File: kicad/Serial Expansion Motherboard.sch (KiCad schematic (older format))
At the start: 0 parts

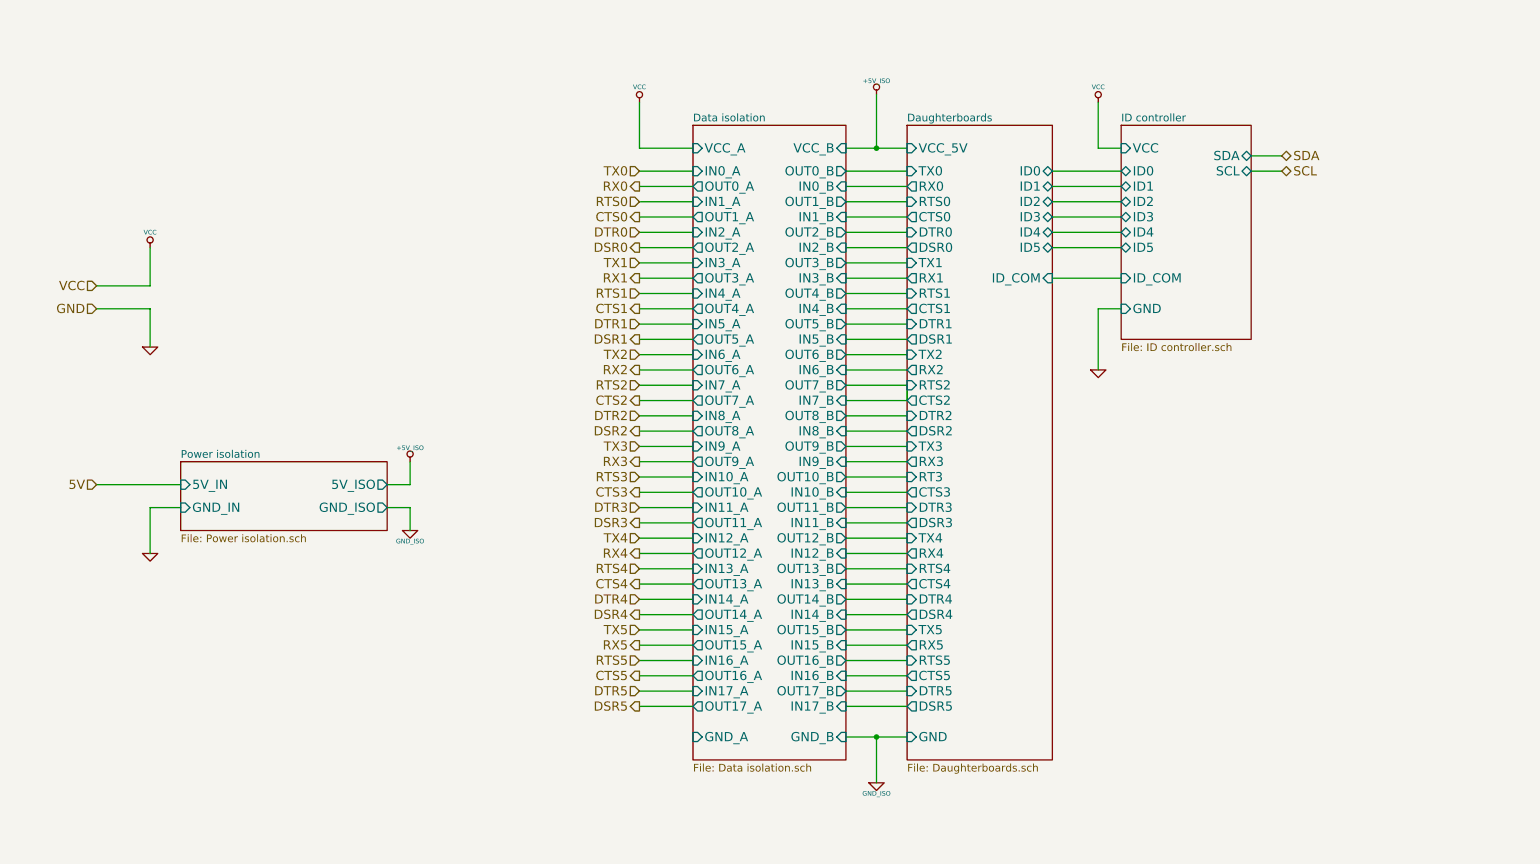
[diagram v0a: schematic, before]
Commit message: Completed data and power isolation sheets
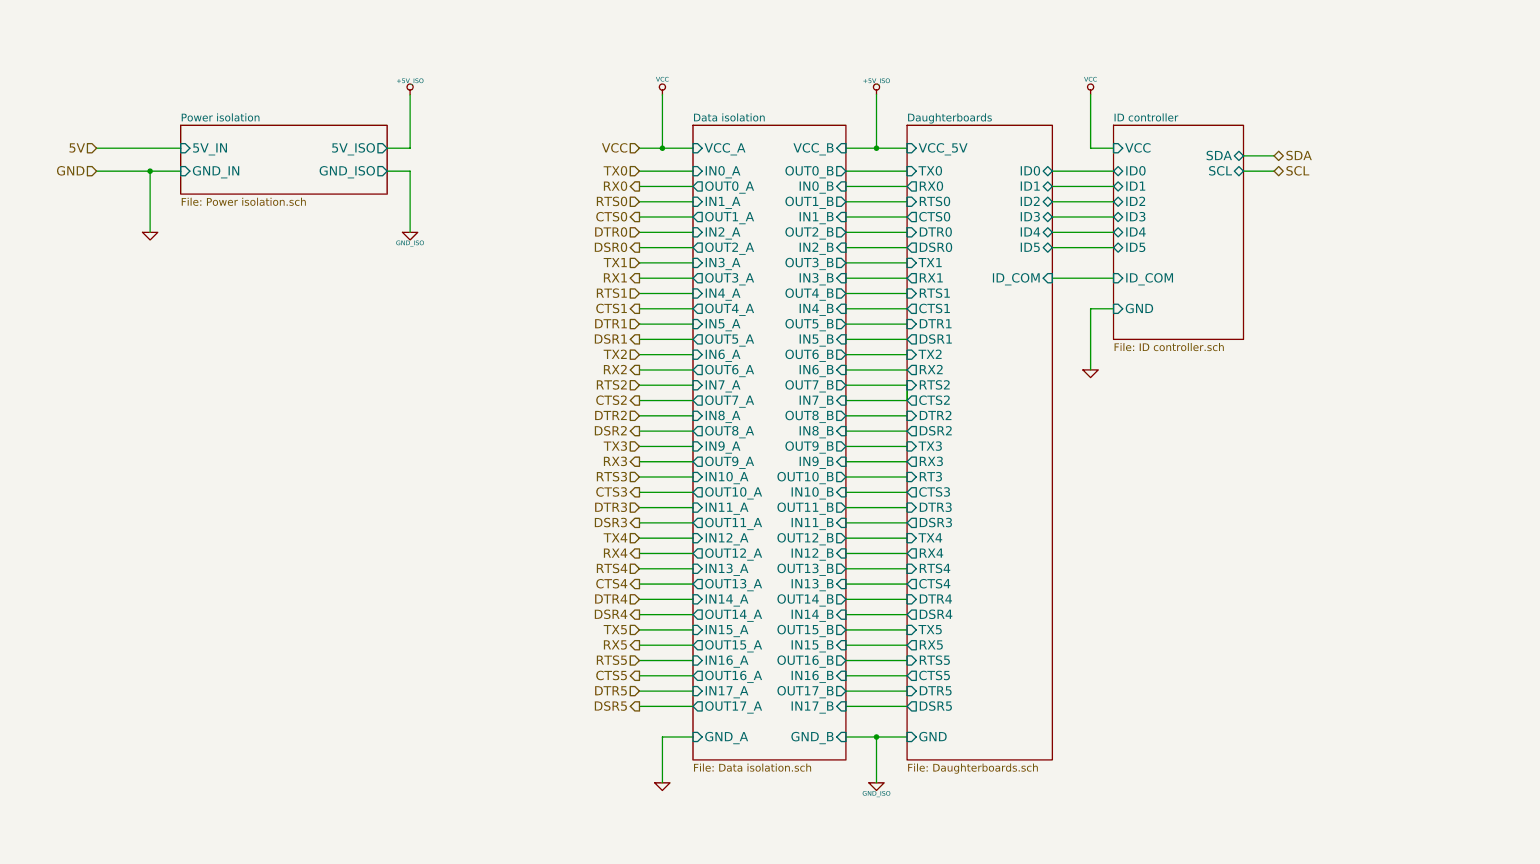
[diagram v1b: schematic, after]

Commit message: ID controller complete, bypass caps added in data isolation
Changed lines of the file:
@@
 LIBS:roe-0505s
 LIBS:si8660
+LIBS:pic16f1704
 LIBS:Main-cache
 EELAYER 27 0
@@
 	5550 5450 5200 5450
 Wire Wire Line
-	5550 1900 5350 1900
-Wire Wire Line
-	5350 1900 5200 1900
+	5200 1900 5550 1900
 Wire Wire Line
 	5550 2150 5200 2150
@@
 	6950 5550 6550 5550
 Wire Wire Line
-	6550 5750 6750 5750
-Wire Wire Line
-	6750 5750 6950 5750
+	6550 5750 6950 5750
 Wire Wire Line
 	7900 2050 8300 2050
@@
 	8150 1900 8150 1550
 Wire Wire Line
-	6550 1900 6750 1900
-Wire Wire Line
-	6750 1900 6950 1900
+	6550 1900 6950 1900
 Connection ~ 6750 1900
 Wire Wire Line
@@
 	1650 1900 2200 1900
 Wire Wire Line
-	1650 2050 2000 2050
-Wire Wire Line
-	2000 2050 2200 2050
+	1650 2050 2200 2050
 Wire Wire Line
 	2000 2050 2000 2450

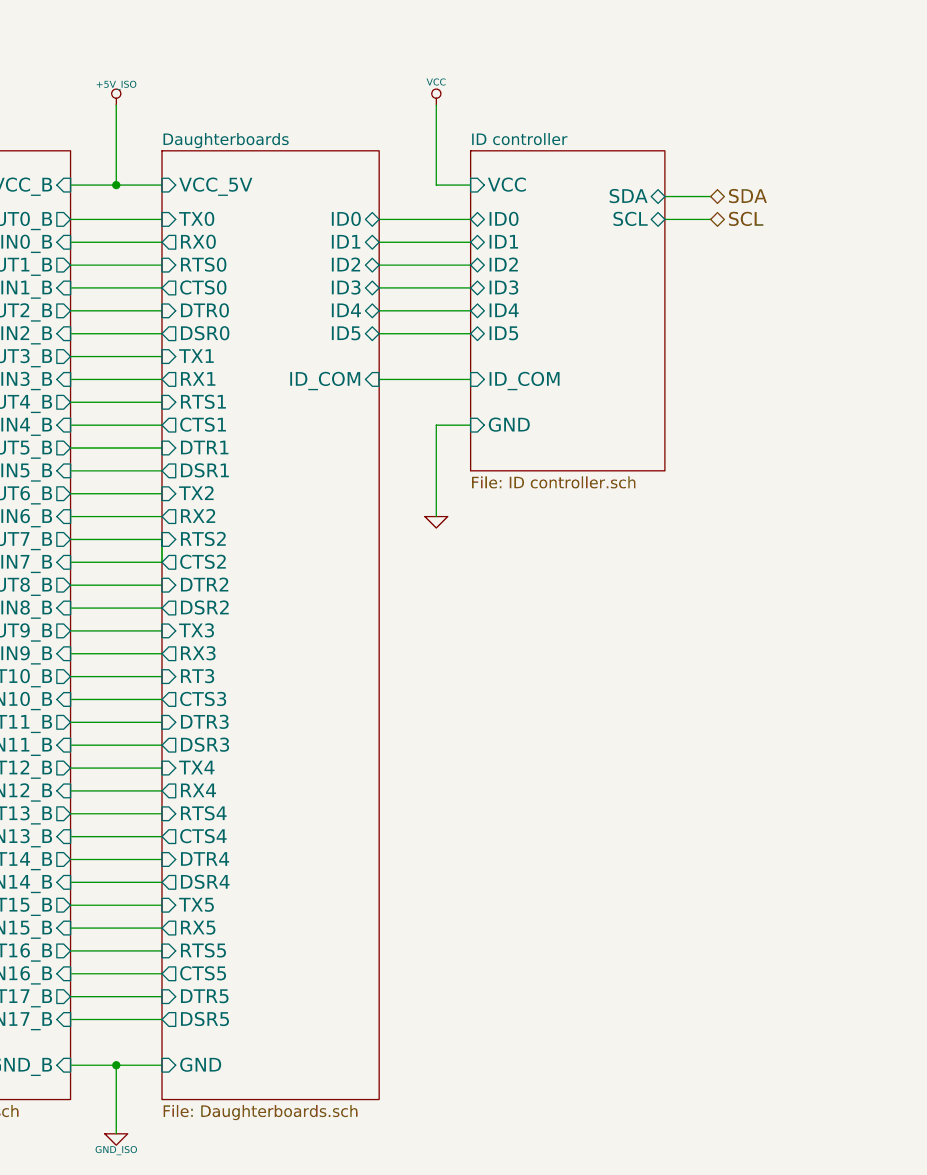
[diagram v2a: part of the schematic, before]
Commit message: ID detection changed from RC to EEPROM based, D.board pinout changed, PIC18F85J94 added
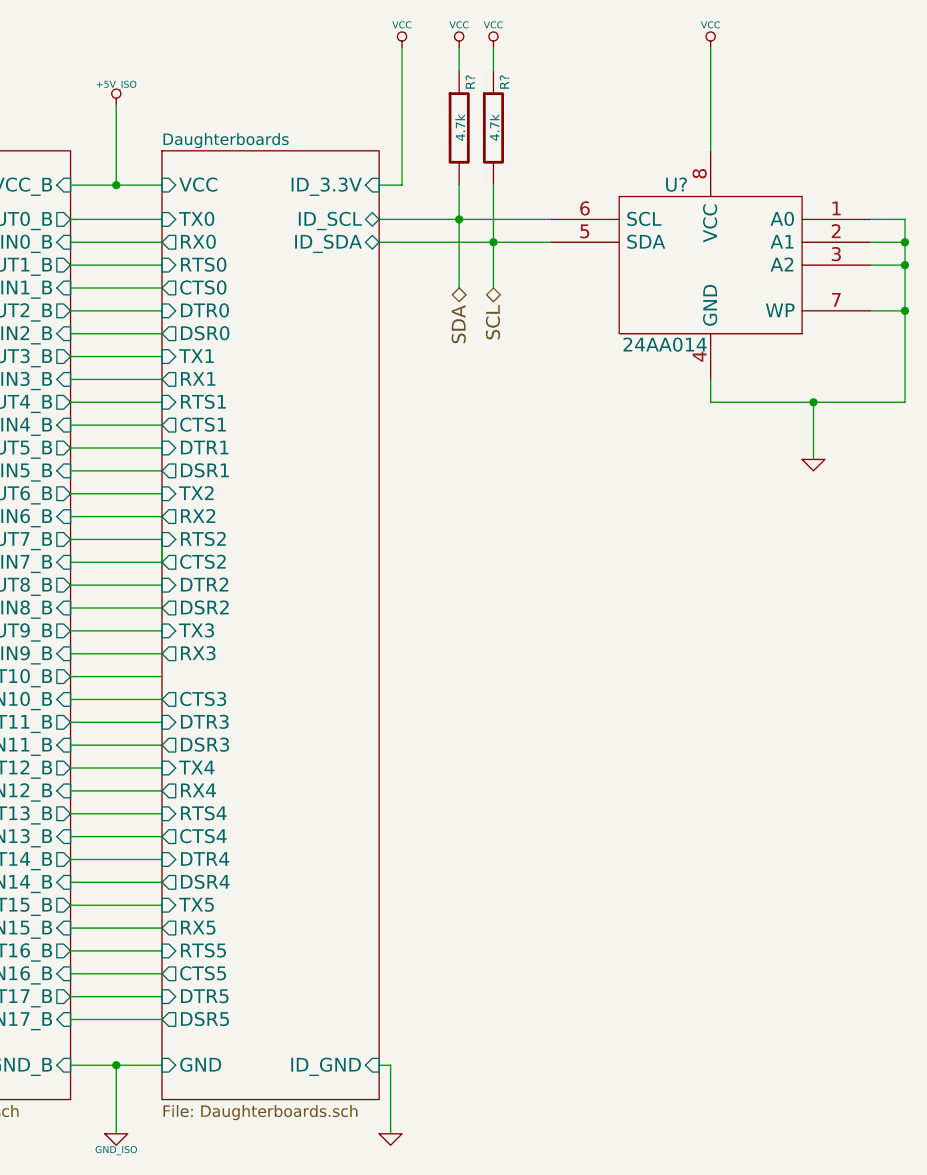
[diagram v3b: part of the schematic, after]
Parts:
- added R? (x2): 4.7k, ~, symbol R
- added U?: 24AA014, ~, symbol 24AA014
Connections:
- net GND: now also U?.1 (A0), U?.2 (A1), U?.3 (A2), U?.4 (GND), U?.7 (WP)
- net SCL: now also R?.2, U?.5 (SDA)
- net SDA: now also R?.2, U?.6 (SCL)
- net VCC: now also R?.1, R?.1, U?.8 (VCC)

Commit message: Completed PIC 18 USB sheet; Motherboard schematic done
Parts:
- added C?: 0.1u, ~, symbol CSMALL
- added R?: 50, ~, symbol R
- R? (x2): value 4.7k -> 2.2k
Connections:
- wire segments 107 -> 124
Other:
- moved on the sheet: R?, U?

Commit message: Netlist DRC pass - fixed pins types, incorrect connections, added PWRFLAGS
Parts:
- gave numbers to parts that had none: 5
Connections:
- wire segments 124 -> 112
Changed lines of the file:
@@
 F2 "5V_IN" I L 1950 2000 60
 F3 "GND_IN" I L 1950 2150 60
-F4 "5V_ISO" O R 3300 2000 60
-F5 "GND_ISO" O R 3300 2150 60
+F4 "5V_OUT" O R 3300 2000 60
+F5 "GND_OUT" O R 3300 2150 60
 $EndSheet
 Text HLabel 1400 2000 0    60   Input ~ 0
@@
 F41 "ID_3.3V" I R 7650 2000 60
 F42 "ID_GND" I R 7650 5850 60
+F43 "RTS3" I L 6700 4150 60
 $EndSheet
 $Comp
-L GND #PWR?
+L GND #PWR401
 U 1 1 53B054FA
 P 1750 2550
-F 0 "#PWR?" H 1750 2550 30  0001 C CNN
+F 0 "#PWR401" H 1750 2550 30  0001 C CNN
 F 1 "GND" H 1750 2480 30  0001 C CNN
 F 2 "" H 1750 2550 60  0000 C CNN
@@
 $EndComp
 $Comp
-L VCC #PWR?
+L VCC #PWR405
 U 1 1 53B14771
 P 5100 1400
-F 0 "#PWR?" H 5100 1500 30  0001 C CNN
+F 0 "#PWR405" H 5100 1500 30  0001 C CNN
 F 1 "VCC" H 5100 1500 30  0000 C CNN
 F 2 "" H 5100 1400 60  0000 C CNN
@@
 $EndComp
 $Comp
-L +5V_ISO #PWR?
+L +5V_ISO #PWR407
 U 1 1 53A78151
 P 6500 1400
-F 0 "#PWR?" H 6500 1490 20  0001 C CNN
+F 0 "#PWR407" H 6500 1490 20  0001 C CNN
 F 1 "+5V_ISO" H 6500 1490 30  0000 C CNN
 F 2 "~" H 6500 1400 60  0000 C CNN
@@
 $EndComp
 $Comp
-L GND_ISO #PWR?
+L GND_ISO #PWR408
 U 1 1 53A7B61B
 P 6500 6400
-F 0 "#PWR?" H 6500 6400 30  0001 C CNN
+F 0 "#PWR408" H 6500 6400 30  0001 C CNN
 F 1 "GND_ISO" H 6500 6330 30  0000 C CNN
 F 2 "~" H 6500 6400 60  0000 C CNN
@@
 $EndComp
 $Comp
-L +5V_ISO #PWR?
+L +5V_ISO #PWR403
 U 1 1 53A80772
 P 3750 1650
-F 0 "#PWR?" H 3750 1740 20  0001 C CNN
+F 0 "#PWR403" H 3750 1740 20  0001 C CNN
 F 1 "+5V_ISO" H 3750 1740 30  0000 C CNN
 F 2 "~" H 3750 1650 60  0000 C CNN
@@
 $EndComp
 $Comp
-L GND_ISO #PWR?
+L GND_ISO #PWR404
 U 1 1 53A80B80
 P 3750 2550
-F 0 "#PWR?" H 3750 2550 30  0001 C CNN
+F 0 "#PWR404" H 3750 2550 30  0001 C CNN
 F 1 "GND_ISO" H 3750 2480 30  0000 C CNN
 F 2 "~" H 3750 2550 60  0000 C CNN
@@
 $EndComp
 $Comp
-L GND #PWR?
+L GND #PWR406
 U 1 1 53AAB6DF
 P 5100 6400
-F 0 "#PWR?" H 5100 6400 30  0001 C CNN
+F 0 "#PWR406" H 5100 6400 30  0001 C CNN
 F 1 "GND" H 5100 6330 30  0001 C CNN
 F 2 "" H 5100 6400 60  0000 C CNN
@@
 	5300 5550 4950 5550
 Wire Wire Line
-	4950 2000 5100 2000
-Wire Wire Line
-	5100 2000 5300 2000
+	4950 2000 5300 2000
 Wire Wire Line
 	5300 2250 4950 2250
@@
 	6700 5650 6300 5650
 Wire Wire Line
-	6300 5850 6500 5850
-Wire Wire Line
-	6500 5850 6700 5850
-Wire Wire Line
-	6300 2000 6500 2000
-Wire Wire Line
-	6500 2000 6700 2000
+	6300 5850 6700 5850
+Wire Wire Line
+	6300 2000 6700 2000
 Connection ~ 6500 2000
 Wire Wire Line
@@
 	1400 2000 1950 2000
 Wire Wire Line
-	1400 2150 1750 2150
-Wire Wire Line
-	1750 2150 1950 2150
+	1400 2150 1950 2150
 Wire Wire Line
 	1750 2150 1750 2550
@@
 Connection ~ 5100 2000
 $Comp
-L 24AA014 U?
+L 24AA014 U401
 U 1 1 53B4C2D2
 P 9250 2350
-F 0 "U?" H 9600 2700 60  0000 C CNN
+F 0 "U401" H 9550 2700 60  0000 C CNN
 F 1 "24AA014" H 9000 2000 60  0000 C CNN
 F 2 "~" H 9250 2350 60  0000 C CNN
@@
 	9950 2150 10100 2150
 Wire Wire Line
-	10100 2150 10100 2250
-Wire Wire Line
-	10100 2250 10100 2350
-Wire Wire Line
-	10100 2350 10100 2550
-Wire Wire Line
-	10100 2550 10100 2950
-Wire Wire Line
-	10100 2950 10100 3200
+	10100 2150 10100 3200
 Wire Wire Line
 	9250 2950 10100 2950
@@
 Connection ~ 10100 2550
 $Comp
-L VCC #PWR?
+L VCC #PWR413
 U 1 1 53B55B31
 P 8550 1400
-F 0 "#PWR?" H 8550 1500 30  0001 C CNN
+F 0 "#PWR413" H 8550 1500 30  0001 C CNN
 F 1 "VCC" H 8550 1500 30  0000 C CNN
 F 2 "" H 8550 1400 60  0000 C CNN
@@
 SCL
 Wire Wire Line
-	7650 2150 8000 2150
-Wire Wire Line
-	8000 2150 8550 2150
-Wire Wire Line
-	7650 2250 8150 2250
-Wire Wire Line
-	8150 2250 8550 2250
-Wire Wire Line
-	8000 2000 8000 2150
-Wire Wire Line
-	8000 2150 8000 2450
+	7650 2150 8550 2150
+Wire Wire Line
+	7650 2250 8550 2250
+Wire Wire Line
+	8000 2000 8000 2450
 Connection ~ 8000 2150
 Connection ~ 8150 2250
 $Comp
-L VCC #PWR?
+L VCC #PWR411
 U 1 1 53B5B188
 P 8000 1400
-F 0 "#PWR?" H 8000 1500 30  0001 C CNN
+F 0 "#PWR411" H 8000 1500 30  0001 C CNN
 F 1 "VCC" H 8000 1500 30  0000 C CNN
 F 2 "" H 8000 1400 60  0000 C CNN
@@
 $EndComp
 $Comp
-L R R?
+L R R402
 U 1 1 53B5BAE2
 P 8150 1750
-F 0 "R?" V 8200 1950 40  0000 C CNN
+F 0 "R402" V 8200 2000 40  0000 C CNN
 F 1 "2.2k" V 8157 1751 40  0000 C CNN
 F 2 "~" V 8080 1750 30  0000 C CNN
@@
 $EndComp
 $Comp
-L R R?
+L R R401
 U 1 1 53B5C204
 P 8000 1750
-F 0 "R?" V 8050 1950 40  0000 C CNN
+F 0 "R401" V 8050 2000 40  0000 C CNN
 F 1 "2.2k" V 8007 1751 40  0000 C CNN
 F 2 "~" V 7930 1750 30  0000 C CNN
@@
 	8000 1500 8000 1400
 $Comp
-L VCC #PWR?
+L VCC #PWR412
 U 1 1 53B5CDEE
 P 8150 1400
-F 0 "#PWR?" H 8150 1500 30  0001 C CNN
+F 0 "#PWR412" H 8150 1500 30  0001 C CNN
 F 1 "VCC" H 8150 1500 30  0000 C CNN
 F 2 "" H 8150 1400 60  0000 C CNN
@@
 	8150 1500 8150 1400
 Wire Wire Line
-	8150 2000 8150 2250
-Wire Wire Line
-	8150 2250 8150 2450
+	8150 2000 8150 2450
 Wire Wire Line
 	9250 1600 9250 1850
 $Comp
-L GND #PWR?
+L GND #PWR415
 U 1 1 53B60430
 P 10100 3200
-F 0 "#PWR?" H 10100 3200 30  0001 C CNN
+F 0 "#PWR415" H 10100 3200 30  0001 C CNN
 F 1 "GND" H 10100 3130 30  0001 C CNN
 F 2 "" H 10100 3200 60  0000 C CNN
@@
 	7750 2000 7750 1400
 $Comp
-L VCC #PWR?
+L VCC #PWR409
 U 1 1 53B6B29A
 P 7750 1400
-F 0 "#PWR?" H 7750 1500 30  0001 C CNN
+F 0 "#PWR409" H 7750 1500 30  0001 C CNN
 F 1 "VCC" H 7750 1500 30  0000 C CNN
 F 2 "" H 7750 1400 60  0000 C CNN
@@
 	7750 5850 7750 6400
 $Comp
-L GND #PWR?
+L GND #PWR410
 U 1 1 53B6D3BC
 P 7750 6400
-F 0 "#PWR?" H 7750 6400 30  0001 C CNN
+F 0 "#PWR410" H 7750 6400 30  0001 C CNN
 F 1 "GND" H 7750 6330 30  0001 C CNN
 F 2 "" H 7750 6400 60  0000 C CNN
@@
 $EndComp
 Wire Wire Line
-	9150 1600 9250 1600
-Wire Wire Line
-	9250 1600 9550 1600
+	9150 1600 9550 1600
 Connection ~ 9250 1600
 Wire Wire Line
@@
 	10100 1600 10100 1850
 $Comp
-L GND #PWR?
+L GND #PWR414
 U 1 1 53B794C3
 P 10100 1850
-F 0 "#PWR?" H 10100 1850 30  0001 C CNN
+F 0 "#PWR414" H 10100 1850 30  0001 C CNN
 F 1 "GND" H 10100 1780 30  0001 C CNN
 F 2 "" H 10100 1850 60  0000 C CNN
@@
 Connection ~ 10100 2950
 $Comp
-L R R?
+L R R403
 U 1 1 53B96826
 P 8900 1600
-F 0 "R?" V 8980 1600 40  0000 C CNN
+F 0 "R403" V 8980 1600 40  0000 C CNN
 F 1 "50" V 8907 1601 40  0000 C CNN
 F 2 "~" V 8830 1600 30  0000 C CNN
@@
 	8550 1600 8550 1400
 $Comp
-L CSMALL C?
+L CSMALL C401
 U 1 1 53B782B2
 P 9650 1600
-F 0 "C?" V 9700 1650 30  0000 L CNN
+F 0 "C401" V 9700 1650 30  0000 L CNN
 F 1 "0.1u" V 9600 1650 30  0000 L CNN
 F 2 "~" H 9650 1600 60  0000 C CNN
@@
 	0    1    1    0
 $EndComp
+$Comp
+L GND_ISO #PWR402
+U 1 1 53C1330A
+P 3200 6300
+F 0 "#PWR402" H 3200 6300 30  0001 C CNN
+F 1 "GND_ISO" H 3200 6230 30  0000 C CNN
+F 2 "~" H 3200 6300 60  0000 C CNN
+F 3 "~" H 3200 6300 60  0000 C CNN
+	1    3200 6300
+	1    0    0    -1
+$EndComp
+$Comp
+L PWR_FLAG #FLG401
+U 1 1 53C14186
+P 3200 6100
+F 0 "#FLG401" H 3200 6195 30  0001 C CNN
+F 1 "PWR_FLAG" H 3200 6280 30  0001 C CNN
+F 2 "" H 3200 6100 60  0000 C CNN
+F 3 "" H 3200 6100 60  0000 C CNN
+	1    3200 6100
+	1    0    0    -1
+$EndComp
+Wire Wire Line
+	3200 6100 3200 6300
+$Comp
+L PWR_FLAG #FLG402
+U 1 1 53C2D351
+P 9250 1600
+F 0 "#FLG402" H 9250 1695 30  0001 C CNN
+F 1 "PWR_FLAG" H 9250 1780 30  0001 C CNN
+F 2 "" H 9250 1600 60  0000 C CNN
+F 3 "" H 9250 1600 60  0000 C CNN
+	1    9250 1600
+	1    0    0    -1
+$EndComp
 $EndSCHEMATC

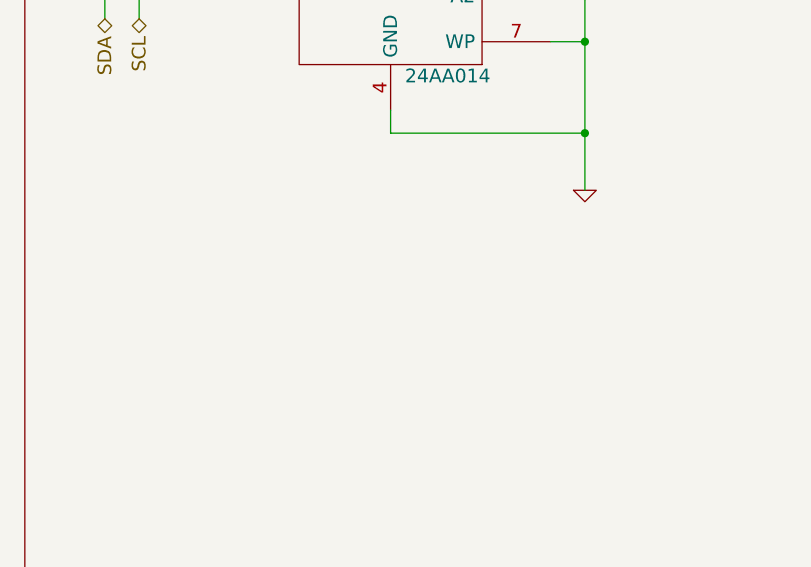
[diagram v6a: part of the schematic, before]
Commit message: Updated notes and sheet names
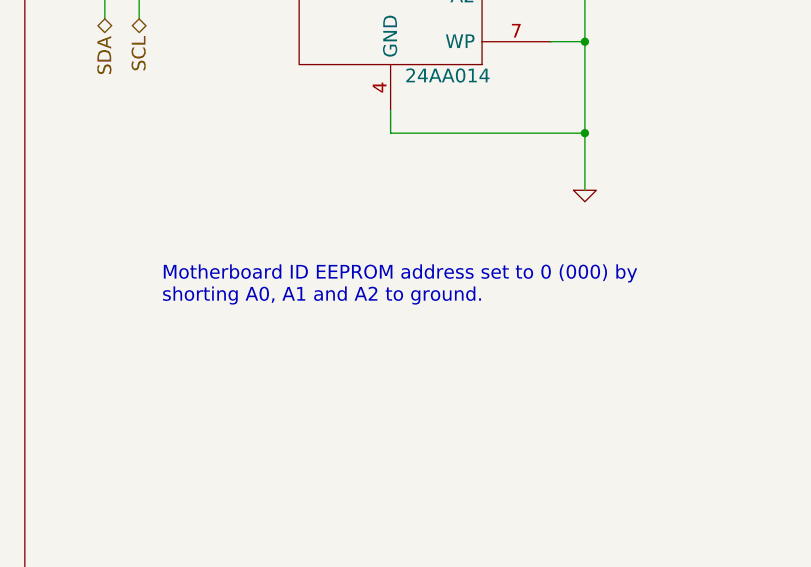
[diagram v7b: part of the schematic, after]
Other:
- note added: "Motherboard ID EEPROM address set to 0 (000) by \nshorting A0, A1 and A2 to ground."
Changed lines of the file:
@@
 encoding utf-8
 Sheet 4 7
-Title ""
+Title "Serial Expansion Module"
 Date "23 jun 2014"
 Rev ""
-Comp ""
+Comp "TimVideos"
 Comment1 ""
 Comment2 ""
@@
 	1    0    0    -1
 $EndComp
+Text Notes 8250 3700 0    60   ~ 0
+Motherboard ID EEPROM address set to 0 (000) by \nshorting A0, A1 and A2 to ground.
 $EndSCHEMATC
